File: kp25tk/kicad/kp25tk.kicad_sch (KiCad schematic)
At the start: 53 parts, among them J1 Host Connector, J2 Wire Wrap Connector, J3 Power In, J4 Row Select In, J5 Column Out, J6 NMI Out, J7 Reset Out, J8 Mode Out, SW0 0, SW1 1, SW10 A, SW11 B, SW12 C, SW13 D, SW14 E, SW15 F, SW16 RUN, SW17 CONT, SW18 ADDR, SW19 READ_DEC, SW2 2, SW20 READ_INC, SW21 WRITE, SW22 MODE, SW23 REG, SW24 MON(NMI), SW25 RESET, SW27 MODE, SW3 3, SW4 4, SW5 5, SW6 6, SW7 7, SW8 8, SW9 9, U1 74LS14

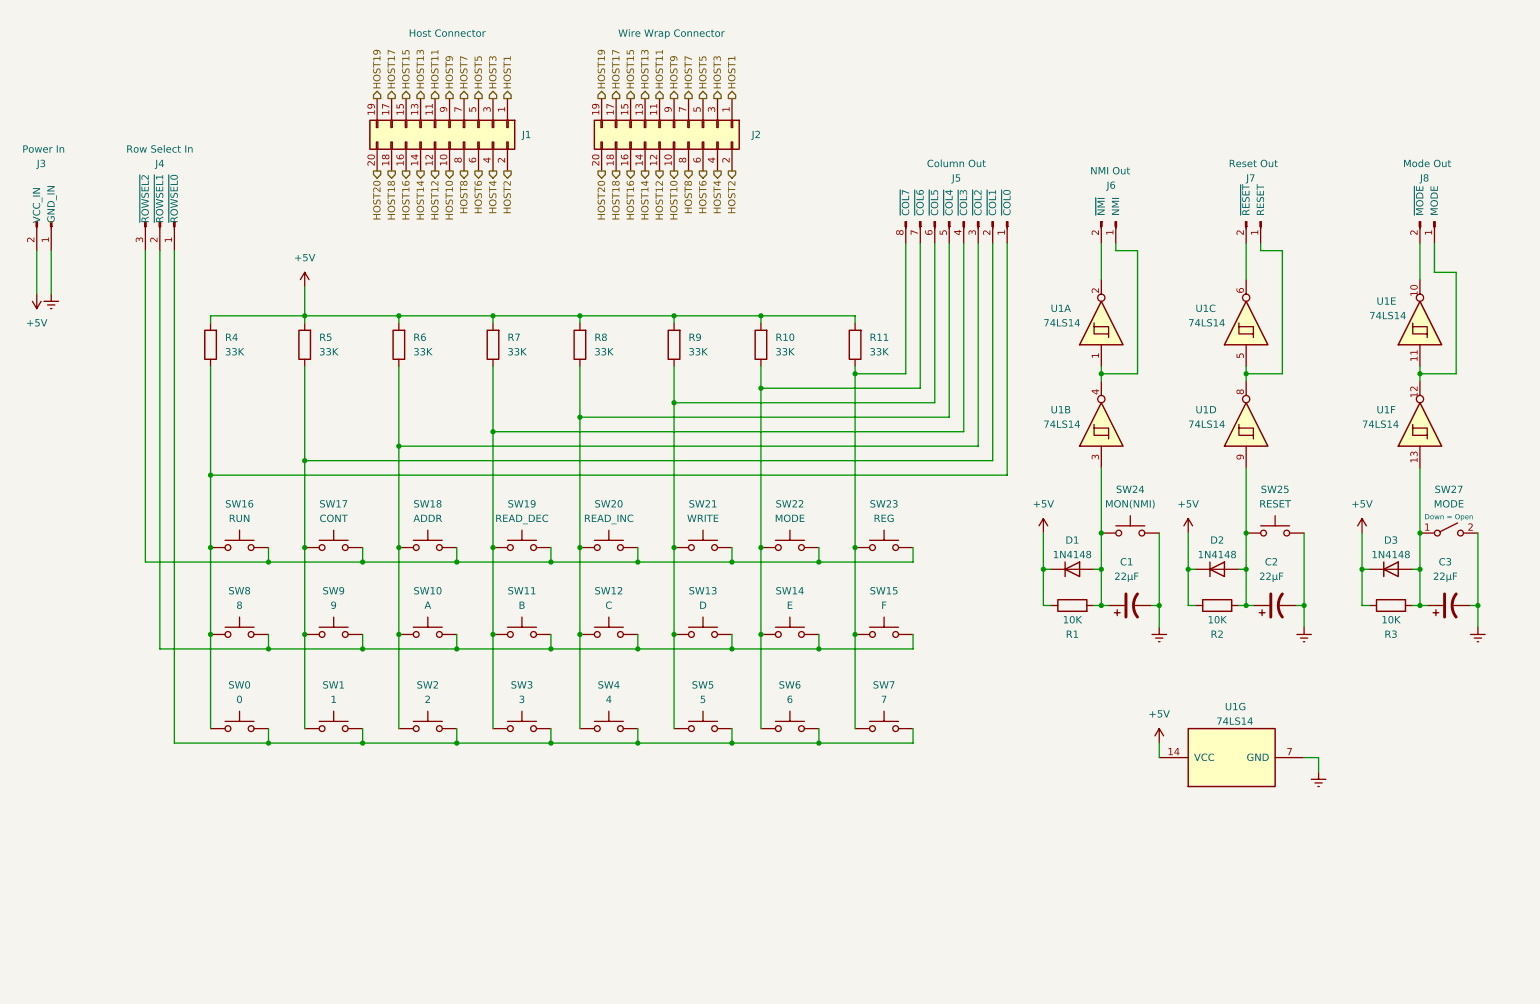
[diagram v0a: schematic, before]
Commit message: kp25tk/: Added diodes (not quite correct), started PCB layout
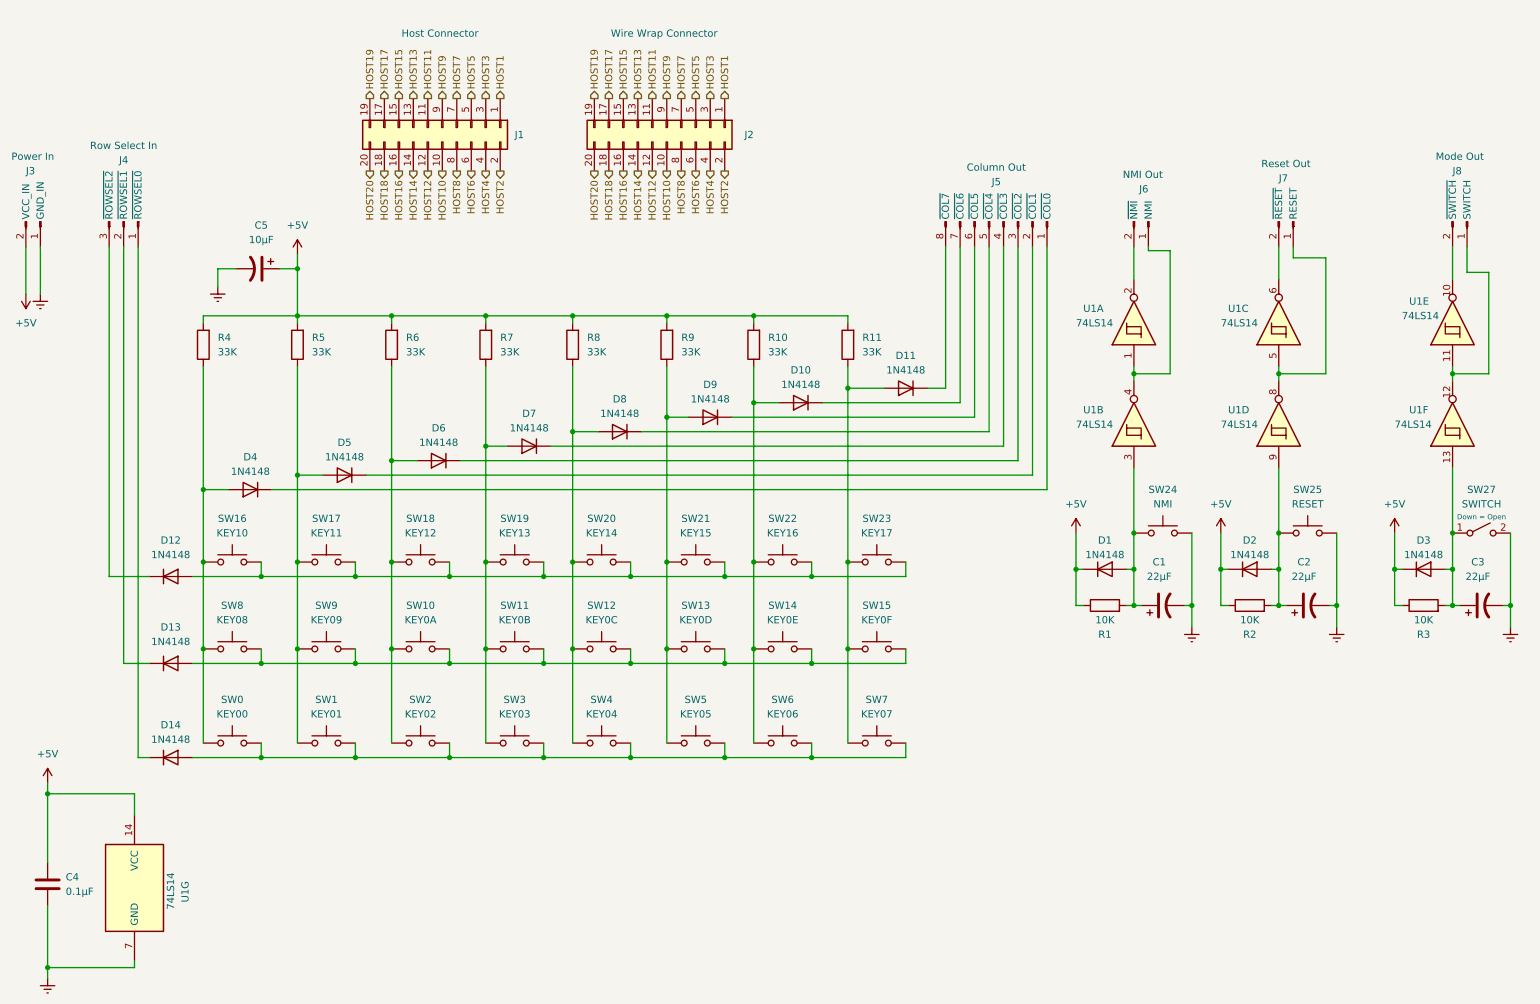
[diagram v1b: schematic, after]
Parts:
- added C4: 0.1µF, Capacitor_THT:C_Disc_D5.0mm_W2.5mm_P5.00mm, symbol Device:C
- added C5: 10µF, Capacitor_THT:CP_Radial_D5.0mm_P2.00mm, symbol Device:C_Polarized_US
- added D10, D11, D12, D13, D14, D4, D5, D6, D7, D8, D9: 1N4148, Diode_THT:D_DO-35_SOD27_P7.62mm_Horizontal, symbol Diode:1N4148
- C1, C2, C3: footprint (none) -> Capacitor_THT:CP_Radial_D5.0mm_P2.00mm
- J1: footprint (none) -> Connector_IDC:IDC-Header_2x10_P2.54mm_Vertical
- J2: footprint (none) -> Connector_PinHeader_2.54mm:PinHeader_2x10_P2.54mm_Vertical
- J3, J6, J7, J8: footprint (none) -> Connector_PinHeader_2.54mm:PinHeader_1x02_P2.54mm_Vertical
- J4: footprint (none) -> Connector_PinHeader_2.54mm:PinHeader_1x03_P2.54mm_Vertical
- J5: footprint (none) -> Connector_PinHeader_2.54mm:PinHeader_1x08_P2.54mm_Vertical
- R1, R10, R11, R2, R3, R4, R5, R6, R7, R8, R9: footprint (none) -> Resistor_THT:R_Axial_DIN0207_L6.3mm_D2.5mm_P10.16mm_Horizontal
- SW0: value 0 -> KEY00; footprint (none) -> Button_Switch_Keyboard:SW_Cherry_MX_1.00u_Plate
- SW1: value 1 -> KEY01; footprint (none) -> Button_Switch_Keyboard:SW_Cherry_MX_1.00u_Plate
- SW10: value A -> KEY0A; footprint (none) -> Button_Switch_Keyboard:SW_Cherry_MX_1.00u_Plate
- SW11: value B -> KEY0B; footprint (none) -> Button_Switch_Keyboard:SW_Cherry_MX_1.00u_Plate
- SW12: value C -> KEY0C; footprint (none) -> Button_Switch_Keyboard:SW_Cherry_MX_1.00u_Plate
- SW13: value D -> KEY0D; footprint (none) -> Button_Switch_Keyboard:SW_Cherry_MX_1.00u_Plate
- SW14: value E -> KEY0E; footprint (none) -> Button_Switch_Keyboard:SW_Cherry_MX_1.00u_Plate
- SW15: value F -> KEY0F; footprint (none) -> Button_Switch_Keyboard:SW_Cherry_MX_1.00u_Plate
- SW16: value RUN -> KEY10; footprint (none) -> Button_Switch_Keyboard:SW_Cherry_MX_1.00u_Plate
- SW17: value CONT -> KEY11; footprint (none) -> Button_Switch_Keyboard:SW_Cherry_MX_1.00u_Plate
- SW18: value ADDR -> KEY12; footprint (none) -> Button_Switch_Keyboard:SW_Cherry_MX_1.00u_Plate
- SW19: value READ_DEC -> KEY13; footprint (none) -> Button_Switch_Keyboard:SW_Cherry_MX_1.00u_Plate
- SW2: value 2 -> KEY02; footprint (none) -> Button_Switch_Keyboard:SW_Cherry_MX_1.00u_Plate
- SW20: value READ_INC -> KEY14; footprint (none) -> Button_Switch_Keyboard:SW_Cherry_MX_1.00u_Plate
- SW21: value WRITE -> KEY15; footprint (none) -> Button_Switch_Keyboard:SW_Cherry_MX_1.00u_Plate
- SW22: value MODE -> KEY16; footprint (none) -> Button_Switch_Keyboard:SW_Cherry_MX_1.00u_Plate
- SW23: value REG -> KEY17; footprint (none) -> Button_Switch_Keyboard:SW_Cherry_MX_1.00u_Plate
- SW24: value MON(NMI) -> NMI; footprint (none) -> Button_Switch_Keyboard:SW_Cherry_MX_1.00u_Plate
- SW25: footprint (none) -> Button_Switch_Keyboard:SW_Cherry_MX_1.00u_Plate
- SW27: value MODE -> SWITCH; footprint (none) -> Button_Switch_Keyboard:SW_Cherry_MX_1.00u_Plate
- SW3: value 3 -> KEY03; footprint (none) -> Button_Switch_Keyboard:SW_Cherry_MX_1.00u_Plate
- SW4: value 4 -> KEY04; footprint (none) -> Button_Switch_Keyboard:SW_Cherry_MX_1.00u_Plate
- SW5: value 5 -> KEY05; footprint (none) -> Button_Switch_Keyboard:SW_Cherry_MX_1.00u_Plate
- SW6: value 6 -> KEY06; footprint (none) -> Button_Switch_Keyboard:SW_Cherry_MX_1.00u_Plate
- SW7: value 7 -> KEY07; footprint (none) -> Button_Switch_Keyboard:SW_Cherry_MX_1.00u_Plate
- SW8: value 8 -> KEY08; footprint (none) -> Button_Switch_Keyboard:SW_Cherry_MX_1.00u_Plate
- SW9: value 9 -> KEY09; footprint (none) -> Button_Switch_Keyboard:SW_Cherry_MX_1.00u_Plate
- U1: footprint (none) -> Package_DIP:DIP-14_W7.62mm_Socket
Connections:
- net +5V: now also C4.2, C5.1
- net Earth: now also C4.1, C5.2
- net at R4.1, SW0.1, SW16.1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: now also D4.2 (A); no longer J5.1 (~{COL0})
- net at SW0.2, SW1.2, SW2.2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: now also D14.2 (A); no longer J4.1 (~{ROWSEL0})
- net at SW10.2, SW11.2, SW12.2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: now also D13.2 (A); no longer J4.2 (~{ROWSEL1})
- net at SW16.2, SW17.2, SW18.2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: now also D12.2 (A); no longer J4.3 (~{ROWSEL2})
- net at R10.1, SW14.1, SW22.1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: now also D10.2 (A); no longer J5.7 (~{COL6})
- net at R9.1, SW13.1, SW21.1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: now also D9.2 (A); no longer J5.6 (~{COL5})
- net at R11.1, SW15.1, SW23.1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: now also D11.2 (A); no longer J5.8 (~{COL7})
- net at R8.1, SW12.1, SW20.1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: now also D8.2 (A); no longer J5.5 (~{COL4})
- net at R5.1, SW1.1, SW17.1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: now also D5.2 (A); no longer J5.2 (~{COL1})
- net at R6.1, SW10.1, SW18.1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: now also D6.2 (A); no longer J5.3 (~{COL2})
- net at R7.1, SW11.1, SW19.1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: now also D7.2 (A); no longer J5.4 (~{COL3})
- new net: D14.1 (K), J4.1 (~{ROWSEL0})
- new net: D13.1 (K), J4.2 (~{ROWSEL1})
- new net: D12.1 (K), J4.3 (~{ROWSEL2})
- new net: D11.1 (K), J5.8 (~{COL7})
- new net: D8.1 (K), J5.5 (~{COL4})
- new net: D4.1 (K), J5.1 (~{COL0})
- new net: D5.1 (K), J5.2 (~{COL1})
- new net: D6.1 (K), J5.3 (~{COL2})
- new net: D7.1 (K), J5.4 (~{COL3})
- new net: D9.1 (K), J5.6 (~{COL5})
- new net: D10.1 (K), J5.7 (~{COL6})
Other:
- moved on the sheet: C1, C2, C3, D1, D2, D3, J1, J2, J3, J4, J5, J6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

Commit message: kp25tk/: Many fixes, and much better and smaller PCB layout (incomplete)
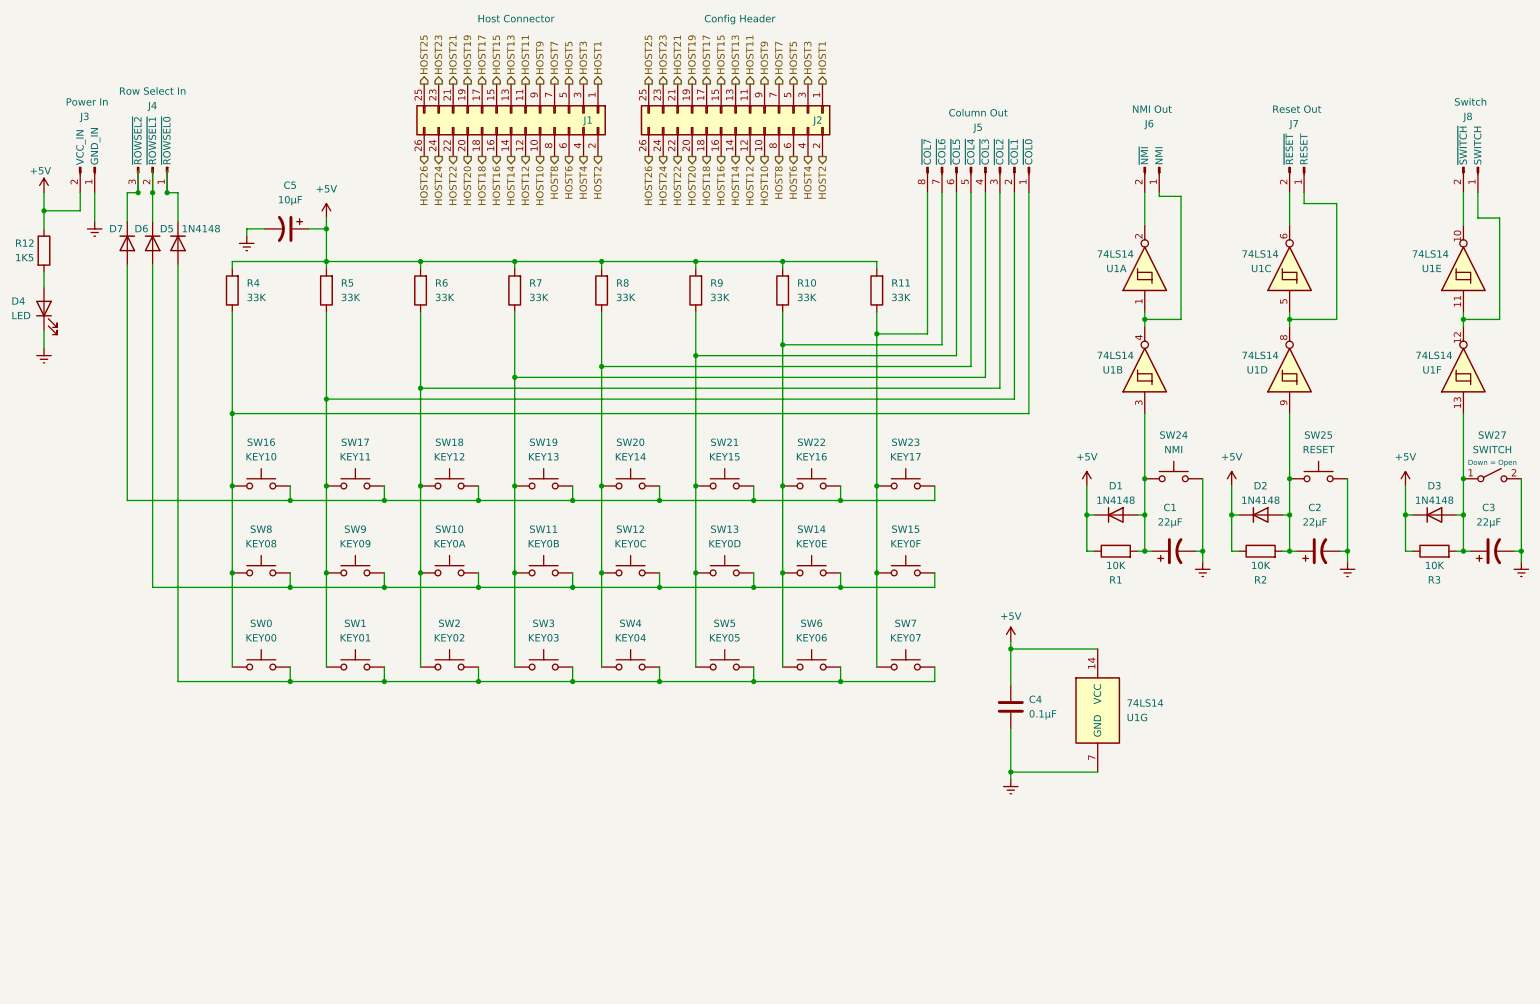
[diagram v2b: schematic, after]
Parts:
- removed D10, D11, D12, D13, D14, D4, D8, D9: 1N4148, Diode_THT:D_DO-35_SOD27_P7.62mm_Horizontal, symbol Diode:1N4148
- added D4: LED, LED_THT:LED_D3.0mm, symbol Device:LED
- added R12: 1K5, Resistor_THT:R_Axial_DIN0207_L6.3mm_D2.5mm_P10.16mm_Horizontal, symbol Device:R
- J1: footprint Connector_IDC:IDC-Header_2x10_P2.54mm_Vertical -> Connector_PinHeader_2.54mm:PinHeader_2x13_P2.54mm_Vertical; symbol Connector_Generic:Conn_02x10_Odd_Even -> Connector_Generic:Conn_02x13_Odd_Even
- J2: value Wire Wrap Connector -> Config Header; footprint Connector_PinHeader_2.54mm:PinHeader_2x10_P2.54mm_Vertical -> Connector_PinHeader_2.54mm:PinHeader_2x13_P2.54mm_Vertical; symbol Connector_Generic:Conn_02x10_Odd_Even -> Connector_Generic:Conn_02x13_Odd_Even
- J8: value Mode Out -> Switch
- SW25: footprint Button_Switch_Keyboard:SW_Cherry_MX_1.00u_Plate -> Button_Switch_THT:SW_PUSH-12mm
- SW27: footprint Button_Switch_Keyboard:SW_Cherry_MX_1.00u_Plate -> Button_Switch_THT:SW_Slide_1P2T_CK_OS102011MS2Q
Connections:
- net +5V: now also R12.1
- net Earth: now also D4.1 (K)
- net at R4.1, SW0.1, SW16.1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: now also J5.1 (~{COL0})
- net at SW0.2, SW1.2, SW2.2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: now also D5.2 (A)
- net at SW10.2, SW11.2, SW12.2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: now also D6.2 (A)
- net at J4.1 (~{ROWSEL0}): now also D5.1 (K)
- net at J4.2 (~{ROWSEL1}): now also D6.1 (K)
- net at J4.3 (~{ROWSEL2}): now also D7.1 (K)
- net at R10.1, SW14.1, SW22.1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: now also J5.7 (~{COL6})
- net at R9.1, SW13.1, SW21.1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: now also J5.6 (~{COL5})
- net at J5.8 (~{COL7}): now also R11.1, SW15.1, SW23.1, SW7.1
- net at R8.1, SW12.1, SW20.1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: now also J5.5 (~{COL4})
- net at R5.1, SW1.1, SW17.1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: now also J5.2 (~{COL1}); no longer D5.2 (A)
- net at SW16.2, SW17.2, SW18.2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: now also D7.2 (A)
- net at R6.1, SW10.1, SW18.1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: now also J5.3 (~{COL2}); no longer D6.2 (A)
- net at J5.4 (~{COL3}): now also R7.1, SW11.1, SW19.1, SW3.1; no longer D7.1 (K)
- new net: D4.2 (A), R12.2
- new net HOST21: J1.21 (Pin_21), J2.21 (Pin_21)
- new net HOST22: J1.22 (Pin_22), J2.22 (Pin_22)
- new net HOST23: J1.23 (Pin_23), J2.23 (Pin_23)
- new net HOST24: J1.24 (Pin_24), J2.24 (Pin_24)
- new net HOST25: J1.25 (Pin_25), J2.25 (Pin_25)
- new net HOST26: J1.26 (Pin_26), J2.26 (Pin_26)
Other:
- moved on the sheet: C1, C2, C3, C4, C5, D1, D2, D3, J3, J4, J5, J7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

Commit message: kp25tk/: v0.0.4 Use resistor array and greatly compactify top of PCB
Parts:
- removed R10, R11, R4, R5, R6, R7, R8, R9: 33K, Resistor_THT:R_Axial_DIN0207_L6.3mm_D2.5mm_P10.16mm_Horizontal, symbol Device:R
- added RN1: 22K, Resistor_THT:R_Array_SIP9, symbol Device:R_Network08_Split
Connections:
- net +5V: now also RN1.1 (R1), RN1.1 (R1), RN1.1 (R1), RN1.1 (R1), RN1.1 (R1), RN1.1 (R1), RN1.1 (R1), RN1.1 (R1)
- net at J5.1 (~{COL0}), SW0.1, SW16.1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: now also RN1.2 (R1.2)
- net at J5.7 (~{COL6}), SW14.1, SW22.1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: now also RN1.8 (R7.2)
- net at J5.6 (~{COL5}), SW13.1, SW21.1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: now also RN1.7 (R6.2)
- net at J5.8 (~{COL7}), SW15.1, SW23.1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: now also RN1.9 (R8.2)
- net at J5.5 (~{COL4}), SW12.1, SW20.1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: now also RN1.6 (R5.2)
- net at J5.2 (~{COL1}), SW1.1, SW17.1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: now also RN1.3 (R2.2)
- net at J5.3 (~{COL2}), SW10.1, SW18.1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: now also RN1.4 (R3.2)
- net at J5.4 (~{COL3}), SW11.1, SW19.1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: now also RN1.5 (R4.2)
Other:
- moved on the sheet: J5
